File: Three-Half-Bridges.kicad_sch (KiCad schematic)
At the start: 37 parts, among them J1 Conn_01x01_Female, J10 Conn_01x02_Male, J11 Conn_01x02_Male, J12 Conn_01x02_Male, J13 Conn_01x02_Male, J2 Conn_01x03_Male, J3 Conn_01x01_Female, J4 Conn_01x01_Female, J5 Conn_01x01_Female, J6 Conn_01x02_Male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

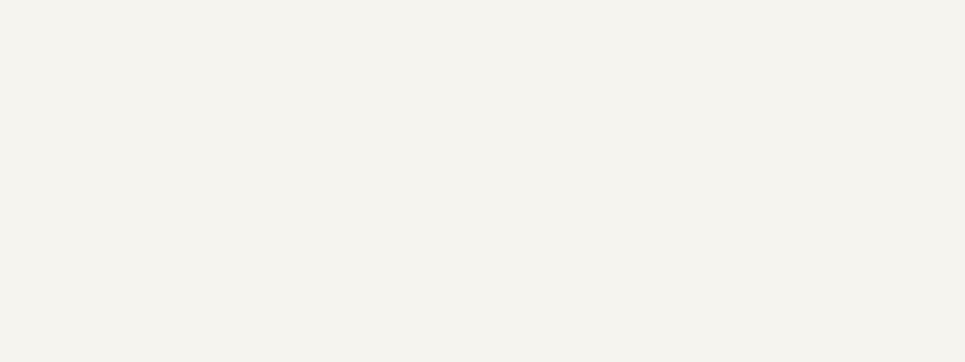
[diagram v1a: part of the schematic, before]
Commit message: added infomation to title block, generated PDF of schematic
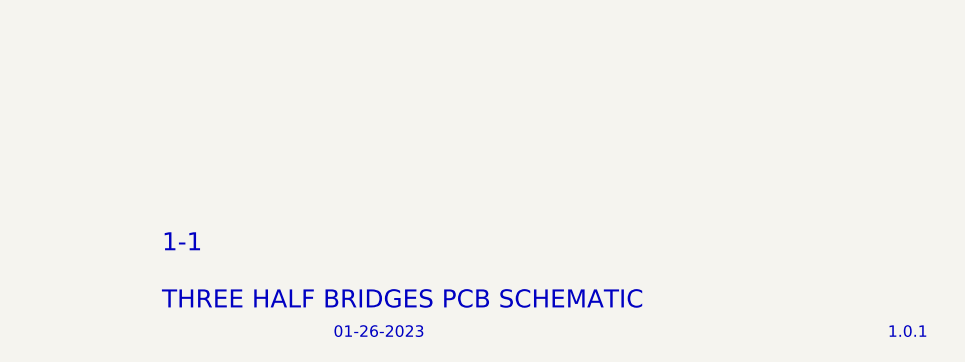
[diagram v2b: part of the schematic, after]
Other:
- note added: "01-26-2023"
- note added: "1-1"
- note added: "1.0.1"
- note added: "THREE HALF BRIDGES PCB SCHEMATIC"
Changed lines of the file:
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@@
     (stroke (width 0) (type default) (color 0 0 0 0))
+  )
+  (text "01-26-2023" (at 189.23 200.025 0)
+    (effects (font (size 1.27 1.27)) (justify left bottom))
+  )
+  (text "1-1" (at 170.18 190.5 0)
+    (effects (font (size 2 2)) (justify left bottom))
+  )
+  (text "1.0.1" (at 250.825 200.025 0)
+    (effects (font (size 1.27 1.27)) (justify left bottom))
+  )
+  (text "THREE HALF BRIDGES PCB SCHEMATIC" (at 170.18 196.85 0)
+    (effects (font (size 2 2)) (justify left bottom))
   )
   (symbol (lib_id "Device:C") (at 50.8 25.4 180) (unit 1)
